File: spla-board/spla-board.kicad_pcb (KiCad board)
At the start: 4 copper layers, 178 x 107 mm, 238 parts, among them J1 USB_B_Micro, J12 J_POWER, J13 J_ANALOG, J14 J_AREF, J15 J_DPULL, J2 J_JTAG, J3 J_BODGE, J4 J_POWER2, J5 J_PPURESET, J6 J_SAMPLE, J7 Barrel_Jack, J8 J_AREF_AMP, U1 LFE5U-45F-BG256, U10 SNES_PPU1, U11 SNES_PPU2, U12 VRAM, U13 VRAM, U14 TLV73311PDBV, U15 74LVC8T245-Q1, U16 74LVC8T245-Q1, U17 74LVC8T245-Q1, U2 FT2232H, U20 74LVC8T245-Q1, U22 74LVC8T245-Q1, U23 74LVC8T245-Q1, U24 74LVC8T245-Q1, U25 74LVC8T245-Q1, U26 74LVC8T245-Q1, U27 74LVC8T245-Q1, U28 74LVC8T245-Q1, U29 74LVC8T245-Q1, U3 93LC66B, U30 74LVC8T245-Q1, U31 74LVC8T245-Q1, U32 74LVC8T245-Q1, U51 ADC1173, U52 ADC1173, U53 ADC1173, U61 LMH6611, U62 LMH6611, U63 LMH6611, U7 ST1S10PHR, U74 LMH6611, U75 LMH6611, U76 TLV73333PDBV, U8 ST1S10PHR, U9 TLV73325PDBV, X1 O252012MEDH4MI

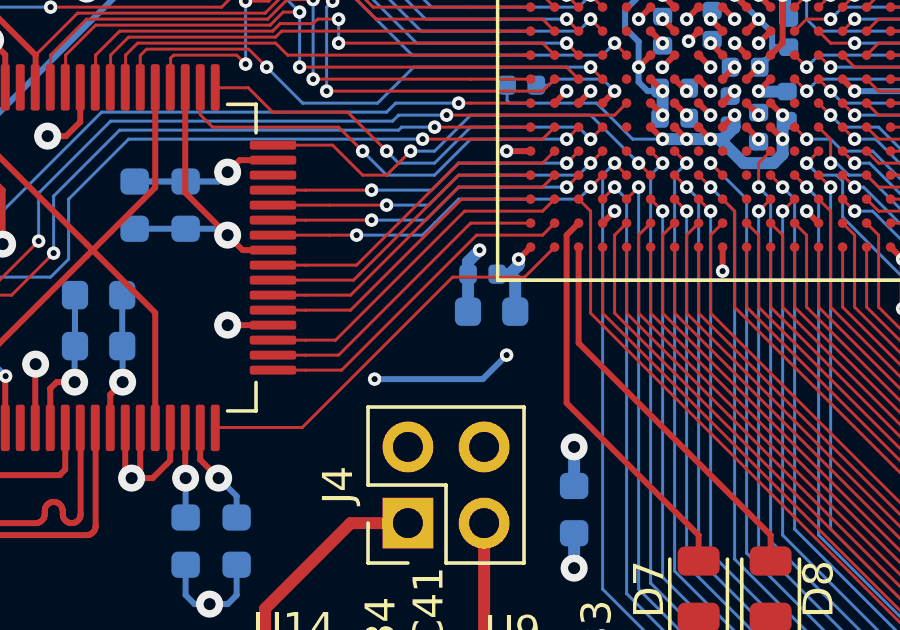
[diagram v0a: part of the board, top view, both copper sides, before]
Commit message: pcb: Tweak +1V1 decoupling capacitors.
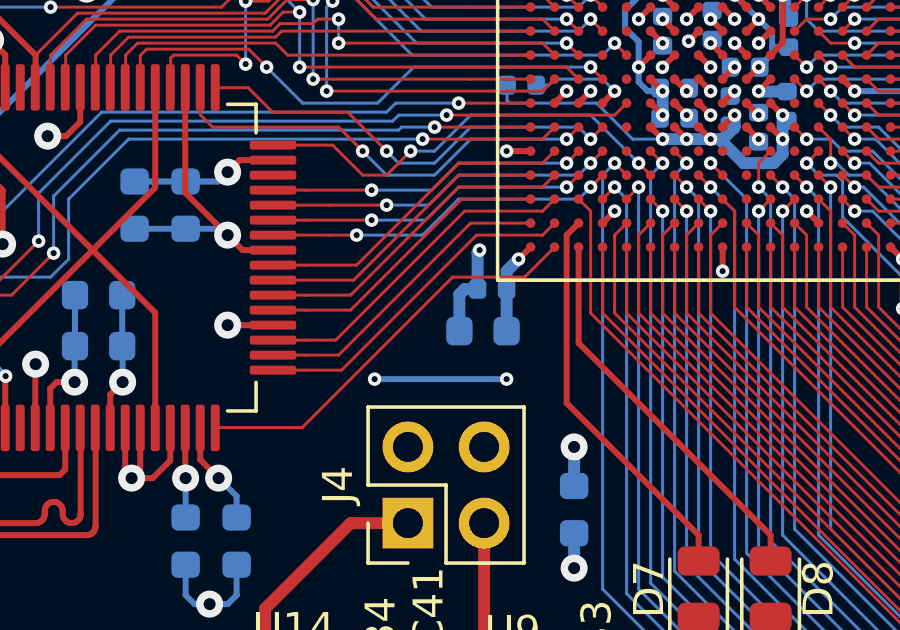
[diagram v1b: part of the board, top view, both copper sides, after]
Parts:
- moved C13 0.71 mm to (89.4, 108.8)
- moved C25 0.59 mm to (89.7, 107.4)
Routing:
- net +1V1: track 41.7 -> 42.8 mm
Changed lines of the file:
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@@
     (thickness 1.6)
     (drawings 59)
-    (tracks 4580)
+    (tracks 4578)
     (zones 0)
     (modules 238)
@@
     (0 F.Cu signal)
     (1 In1.Cu power hide)
-    (2 In2.Cu power hide)
+    (2 In2.Cu power)
     (31 B.Cu signal)
     (32 B.Adhes user)
@@
   )
   (setup
-    (last_trace_width 0.2)
+    (last_trace_width 0.4)
     (user_trace_width 0.1)
     (user_trace_width 0.2)
@@
   )
   (module Capacitor_SMD:C_0402_1005Metric (layer B.Cu)
-    (at 89.4 106.9)
+    (at 89.715 107.4)
     (descr "Capacitor SMD 0402 (1005 Metric), square (rectangular) end terminal, IPC_7351 nominal, (Body size source: http://www.tortai-tech.com/upload/download/2011102023233369053.pdf), generated with kicad-footprint-generator")
     (tags capacitor)
@@
   )
   (module Capacitor_SMD:C_0603_1608Metric (layer B.Cu)
-    (at 89.7 108.15)
+    (at 89.4125 108.8)
     (descr "Capacitor SMD 0603 (1608 Metric), square (rectangular) end terminal, IPC_7351 nominal, (Body size source: http://www.tortai-tech.com/upload/download/2011102023233369053.pdf), generated with kicad-footprint-generator")
     (tags capacitor)
@@
   (gr_line (start 40 155) (end 218 155) (layer Edge.Cuts) (width 0.05))
   (via (at 147.3 129.7) (size 0.9) (drill 0.4) (layers F.Cu B.Cu) (net 1))
-  (via (at 145.7 129.7) (size 0.9) (drill 0.4) (layers F.Cu B.Cu) (net 2))
   (via (at 86 144) (size 0.9) (drill 0.4) (layers F.Cu B.Cu) (net 1))
   (via (at 85 144) (size 0.9) (drill 0.4) (layers F.Cu B.Cu) (net 1))
@@
   (segment (start 98.615 100.815) (end 98.6 100.8) (width 0.4) (layer B.Cu) (net 1))
   (segment (start 99.55 100.815) (end 98.615 100.815) (width 0.4) (layer B.Cu) (net 1))
-  (segment (start 90.6 106.4) (end 90.6 106.6) (width 0.4) (layer B.Cu) (net 1))
-  (segment (start 90.3 106.9) (end 89.885 106.9) (width 0.4) (layer B.Cu) (net 1))
-  (segment (start 90.6 106.6) (end 90.3 106.9) (width 0.4) (layer B.Cu) (net 1))
-  (segment (start 90.4875 107.0875) (end 90.4875 108.15) (width 0.4) (layer B.Cu) (net 1))
-  (segment (start 90.3 106.9) (end 90.4875 107.0875) (width 0.4) (layer B.Cu) (net 1))
   (via (at 92.45 116.7) (size 0.9) (drill 0.4) (layers F.Cu B.Cu) (net 1))
   (segment (start 92.45 115.5375) (end 92.45 116.7) (width 0.4) (layer B.Cu) (net 1))
@@
   (segment (start 154.525 55.625) (end 155.45 55.625) (width 0.2) (layer B.Cu) (net 1))
   (segment (start 154.2 55.95) (end 154.525 55.625) (width 0.2) (layer B.Cu) (net 1))
+  (segment (start 90.2 107.4) (end 90.2 108.8) (width 0.4) (layer B.Cu) (net 1))
+  (segment (start 90.2 106.8) (end 90.6 106.4) (width 0.4) (layer B.Cu) (net 1))
+  (segment (start 90.2 107.4) (end 90.2 106.8) (width 0.4) (layer B.Cu) (net 1))
+  (via (at 145.7 129.7) (size 0.9) (drill 0.4) (layers F.Cu B.Cu) (net 2))
   (segment (start 85.8 110.4) (end 85.8 110.4) (width 0.2) (layer B.Cu) (net 2))
-  (segment (start 89.4 110.4) (end 90.2 109.6) (width 0.2) (layer B.Cu) (net 2))
-  (via (at 90.2 109.6) (size 0.45) (drill 0.2) (layers F.Cu B.Cu) (net 2))
-  (segment (start 85.8 110.4) (end 89.4 110.4) (width 0.2) (layer B.Cu) (net 2))
   (via (at 85.8 110.4) (size 0.45) (drill 0.2) (layers F.Cu B.Cu) (net 2))
   (via (at 96.2 102.4) (size 0.45) (drill 0.2) (layers F.Cu B.Cu) (net 2))
@@
   (via (at 129.9 66.3) (size 0.9) (drill 0.4) (layers F.Cu B.Cu) (net 2))
   (segment (start 131.3125 66.3) (end 129.9 66.3) (width 0.2) (layer B.Cu) (net 2))
+  (segment (start 90.2 110.4) (end 85.8 110.4) (width 0.2) (layer B.Cu) (net 2))
+  (via (at 90.2 110.4) (size 0.45) (drill 0.2) (layers F.Cu B.Cu) (net 2))
   (segment (start 71.0625 102.6) (end 70 102.6) (width 0.2) (layer F.Cu) (net 3))
   (segment (start 70 102.6) (end 69.2125 101.8125) (width 0.2) (layer F.Cu) (net 3))
@@
   (segment (start 94.6 101.6) (end 92.2 101.6) (width 0.4) (layer In2.Cu) (net 18))
   (segment (start 92.2 101.6) (end 89.3 104.5) (width 0.4) (layer In2.Cu) (net 18))
-  (segment (start 88.915 106.485) (end 88.915 106.9) (width 0.4) (layer B.Cu) (net 18))
-  (segment (start 89.3 106.1) (end 88.915 106.485) (width 0.4) (layer B.Cu) (net 18))
-  (segment (start 88.915 108.085) (end 88.9 108.1) (width 0.4) (layer B.Cu) (net 18))
-  (segment (start 88.915 106.9) (end 88.915 108.085) (width 0.4) (layer B.Cu) (net 18))
   (segment (start 99.05 98.85) (end 98.6 98.4) (width 0.2) (layer B.Cu) (net 18))
   (segment (start 98.6 100) (end 99.05 99.55) (width 0.2) (layer B.Cu) (net 18))
@@
   (segment (start 95.75 97.25) (end 97.45 97.25) (width 0.2) (layer B.Cu) (net 18))
   (segment (start 95.315 96.815) (end 95.75 97.25) (width 0.2) (layer B.Cu) (net 18))
+  (segment (start 89.23 106.17) (end 89.23 107.4) (width 0.4) (layer B.Cu) (net 18))
+  (segment (start 89.3 106.1) (end 89.23 106.17) (width 0.4) (layer B.Cu) (net 18))
+  (segment (start 89.23 107.4) (end 88.8 107.4) (width 0.4) (layer B.Cu) (net 18))
+  (segment (start 88.625 107.575) (end 88.625 108.8) (width 0.4) (layer B.Cu) (net 18))
+  (segment (start 88.8 107.4) (end 88.625 107.575) (width 0.4) (layer B.Cu) (net 18))
   (via (at 154.7 83.6) (size 0.45) (drill 0.2) (layers F.Cu B.Cu) (net 19))
   (segment (start 157 83.51) (end 154.79 83.51) (width 0.2) (layer F.Cu) (net 19))

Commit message: schematic/pch: Remove '-Q1' suffix from 74LVC8T245 chips.
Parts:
- U15, U16, U17, U20, U22, U23, U24, U25, U26, U27, U28, U29, U30, U31, U32: value 74LVC8T245-Q1 -> 74LVC8T245
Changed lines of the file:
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@@
     (0 F.Cu signal)
     (1 In1.Cu power hide)
-    (2 In2.Cu power)
+    (2 In2.Cu power hide)
     (31 B.Cu signal)
     (32 B.Adhes user)
@@
   )
   (setup
-    (last_trace_width 0.4)
+    (last_trace_width 0.1)
     (user_trace_width 0.1)
     (user_trace_width 0.2)
@@
       (effects (font (size 1 1) (thickness 0.15)) (justify mirror))
     )
-    (fp_text value 74LVC8T245-Q1 (at 0 -4.95) (layer B.Fab)
+    (fp_text value 74LVC8T245 (at 0 -4.95) (layer B.Fab)
       (effects (font (size 1 1) (thickness 0.15)) (justify mirror))
     )
@@
       (effects (font (size 1 1) (thickness 0.15)) (justify mirror))
     )
-    (fp_text value 74LVC8T245-Q1 (at 0 -4.95) (layer B.Fab)
+    (fp_text value 74LVC8T245 (at 0 -4.95) (layer B.Fab)
       (effects (font (size 1 1) (thickness 0.15)) (justify mirror))
     )
@@
       (effects (font (size 1 1) (thickness 0.15)) (justify mirror))
     )
-    (fp_text value 74LVC8T245-Q1 (at 0 -4.95) (layer B.Fab)
+    (fp_text value 74LVC8T245 (at 0 -4.95) (layer B.Fab)
       (effects (font (size 1 1) (thickness 0.15)) (justify mirror))
     )
@@
       (effects (font (size 1 1) (thickness 0.15)) (justify mirror))
     )
-    (fp_text value 74LVC8T245-Q1 (at 0 -4.95 90) (layer B.Fab)
+    (fp_text value 74LVC8T245 (at 0 -4.95 90) (layer B.Fab)
       (effects (font (size 1 1) (thickness 0.15)) (justify mirror))
     )
@@
       (effects (font (size 1 1) (thickness 0.15)) (justify mirror))
     )
-    (fp_text value 74LVC8T245-Q1 (at 0 -4.95) (layer B.Fab)
+    (fp_text value 74LVC8T245 (at 0 -4.95) (layer B.Fab)
       (effects (font (size 1 1) (thickness 0.15)) (justify mirror))
     )
@@
       (effects (font (size 1 1) (thickness 0.15)) (justify mirror))
     )
-    (fp_text value 74LVC8T245-Q1 (at 0 -4.95) (layer B.Fab)
+    (fp_text value 74LVC8T245 (at 0 -4.95) (layer B.Fab)
       (effects (font (size 1 1) (thickness 0.15)) (justify mirror))
     )
@@
       (effects (font (size 1 1) (thickness 0.15)) (justify mirror))
     )
-    (fp_text value 74LVC8T245-Q1 (at 0 -4.95 90) (layer B.Fab)
+    (fp_text value 74LVC8T245 (at 0 -4.95 90) (layer B.Fab)
       (effects (font (size 1 1) (thickness 0.15)) (justify mirror))
     )
@@
       (effects (font (size 1 1) (thickness 0.15)) (justify mirror))
     )
-    (fp_text value 74LVC8T245-Q1 (at 0 -4.95) (layer B.Fab)
+    (fp_text value 74LVC8T245 (at 0 -4.95) (layer B.Fab)
       (effects (font (size 1 1) (thickness 0.15)) (justify mirror))
     )
@@
       (effects (font (size 1 1) (thickness 0.15)) (justify mirror))
     )
-    (fp_text value 74LVC8T245-Q1 (at 0 -4.95) (layer B.Fab)
+    (fp_text value 74LVC8T245 (at 0 -4.95) (layer B.Fab)
       (effects (font (size 1 1) (thickness 0.15)) (justify mirror))
     )
@@
       (effects (font (size 1 1) (thickness 0.15)) (justify mirror))
     )
-    (fp_text value 74LVC8T245-Q1 (at 0 -4.95) (layer B.Fab)
+    (fp_text value 74LVC8T245 (at 0 -4.95) (layer B.Fab)
       (effects (font (size 1 1) (thickness 0.15)) (justify mirror))
     )
@@
       (effects (font (size 1 1) (thickness 0.15)) (justify mirror))
     )
-    (fp_text value 74LVC8T245-Q1 (at 0 -4.95) (layer B.Fab)
+    (fp_text value 74LVC8T245 (at 0 -4.95) (layer B.Fab)
       (effects (font (size 1 1) (thickness 0.15)) (justify mirror))
     )
@@
       (effects (font (size 1 1) (thickness 0.15)) (justify mirror))
     )
-    (fp_text value 74LVC8T245-Q1 (at 0 -4.95) (layer B.Fab)
+    (fp_text value 74LVC8T245 (at 0 -4.95) (layer B.Fab)
       (effects (font (size 1 1) (thickness 0.15)) (justify mirror))
     )
@@
       (effects (font (size 1 1) (thickness 0.15)) (justify mirror))
     )
-    (fp_text value 74LVC8T245-Q1 (at 0 -4.95 90) (layer B.Fab)
+    (fp_text value 74LVC8T245 (at 0 -4.95 90) (layer B.Fab)
       (effects (font (size 1 1) (thickness 0.15)) (justify mirror))
     )
@@
       (effects (font (size 1 1) (thickness 0.15)) (justify mirror))
     )
-    (fp_text value 74LVC8T245-Q1 (at 0 -4.95) (layer B.Fab)
+    (fp_text value 74LVC8T245 (at 0 -4.95) (layer B.Fab)
       (effects (font (size 1 1) (thickness 0.15)) (justify mirror))
     )
@@
       (effects (font (size 1 1) (thickness 0.15)) (justify mirror))
     )
-    (fp_text value 74LVC8T245-Q1 (at 0 -4.95) (layer B.Fab)
+    (fp_text value 74LVC8T245 (at 0 -4.95) (layer B.Fab)
       (effects (font (size 1 1) (thickness 0.15)) (justify mirror))
     )

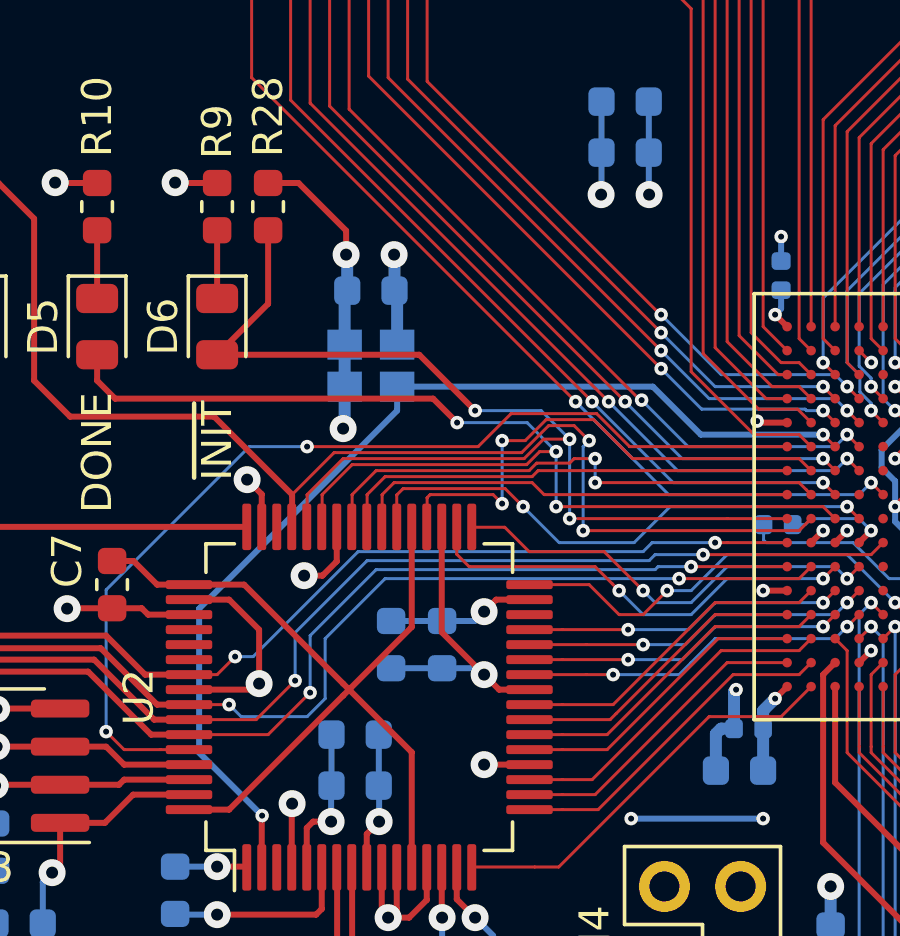
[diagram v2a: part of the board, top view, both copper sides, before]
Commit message: schematic/pcb: Swap oscillator for FOX924 equivalent.
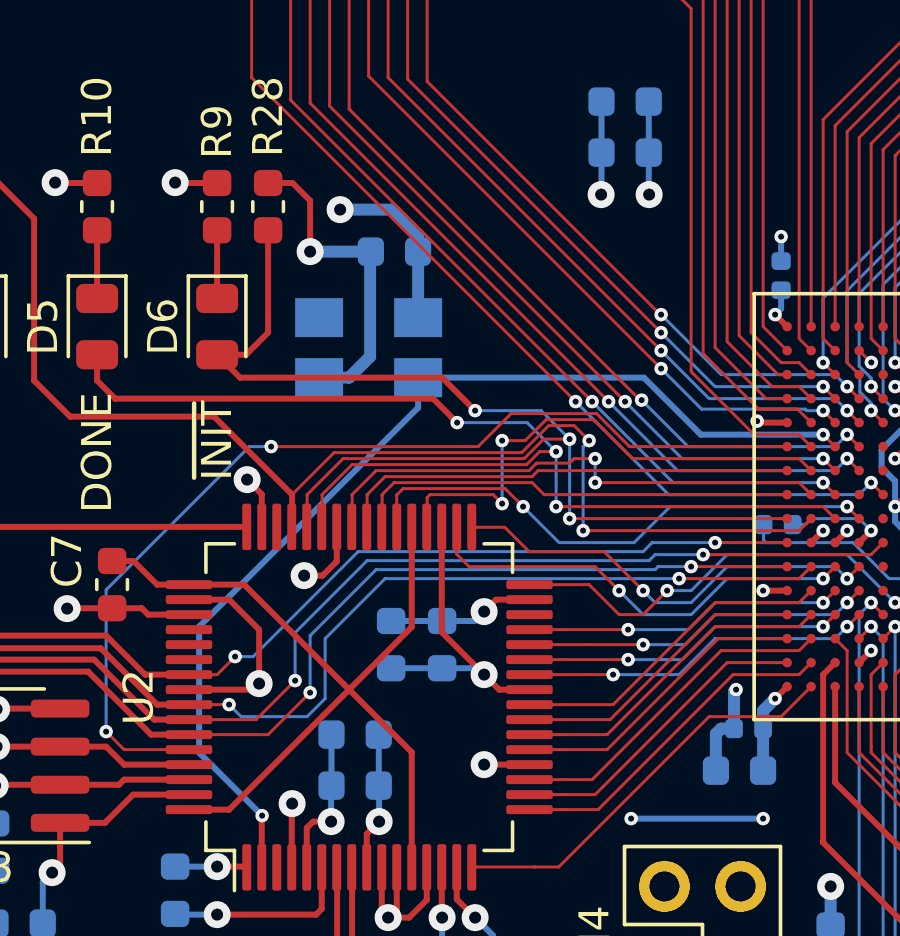
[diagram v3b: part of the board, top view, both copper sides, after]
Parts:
- R121: value 1.64k, 1% -> 1.65k, 1%
- R2, R4, R5: value 10K -> 10k
- R3: value 2.2K -> 2.2k
- R6: value 12K -> 12k
- R7: value 1K -> 1k
- X1: value O252012MEDH4MI -> FT5HNBPK12.0-T1; footprint Crystal:Crystal_SMD_2520-4Pin_2.5x2.0mm -> Crystal:Crystal_SMD_5032-4Pin_5.0x3.2mm
- moved C2 1.52 mm to (77.9, 91.5)
- moved X1 0.60 mm to (77.0, 94.7)
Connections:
- X1 pad 1: +3V3 -> Net-(X1-Pad1)
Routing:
- net GND: track 486.1 -> 488.7 mm
- net +3V3: track 172.4 -> 173.3 mm, vias 51 -> 50
- net ~INIT: track 38.3 -> 38.8 mm

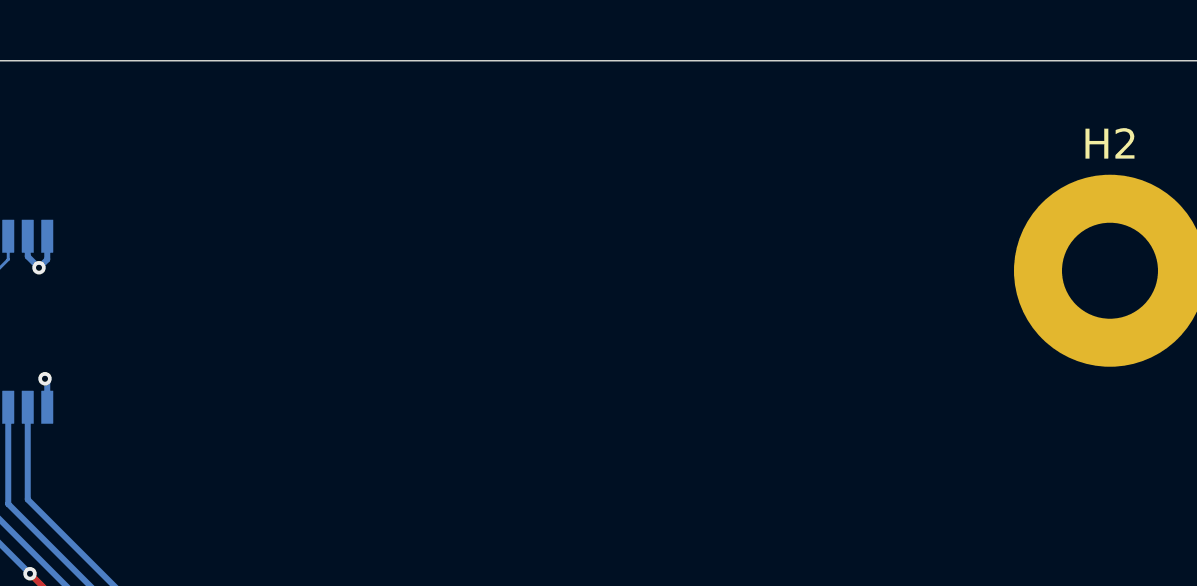
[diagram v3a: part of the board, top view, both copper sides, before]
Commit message: pcb: Add trivial traceability markings.
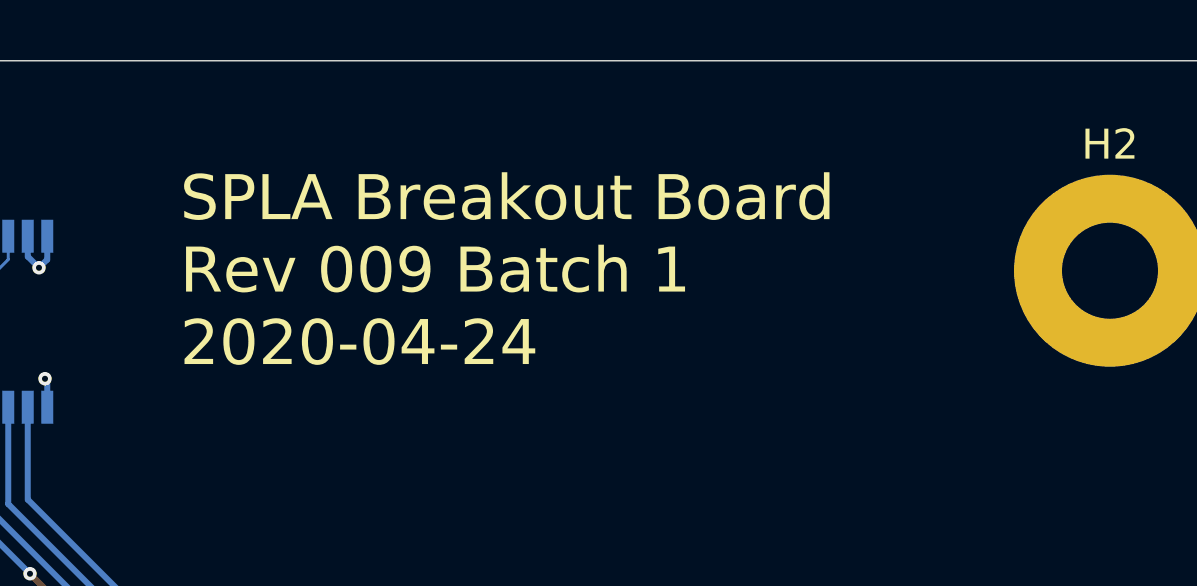
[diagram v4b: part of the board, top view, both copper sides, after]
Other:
- board text added: "SPLA Breakout Board Rev 009 Batch 1 2020-04-24"
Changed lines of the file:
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@@
   (general
     (thickness 1.6)
-    (drawings 59)
+    (drawings 60)
     (tracks 4575)
     (zones 0)
@@
     )
   )
+  (gr_text "SPLA Breakout Board\nRev 009 Batch 1\n2020-04-24" (at 180 55) (layer F.SilkS)
+    (effects (font (size 1.5 1.5) (thickness 0.2)) (justify left))
+  )
   (gr_line (start 101.4 103.6) (end 93.4 103.6) (layer B.SilkS) (width 0.12))
